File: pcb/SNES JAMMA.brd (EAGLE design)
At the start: 66 x 63.5 mm, 10 parts, among them P1-JAMMA-A PLAYER 1 JAMMA, P2-JAMMA-A PLAYER 2 JAMMA

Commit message: v1.0 PCB and Schematics files
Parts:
- removed P1-JAMMA-A: PLAYER 1 JAMMA, con-amp:10X05MTA
- removed P1-JAMMA-B, P2-JAMMA-B: (no value), con-amp:10X06MTA
- removed P2-JAMMA-A: PLAYER 2 JAMMA, con-amp:10X05MTA
- added J1: 12V POWER, con-amp:10X02MTA
- added J2: (no value), con-amp:10X03MTA
- added JAMMA: 057-040-1, con-panduit:057-040-1
- moved CPS1-KICK 59.5 mm to (8.89, 24.1), turned to 90 degrees
- moved EZ-KICK 52.6 mm to (8.89, 49.5), turned to 90 degrees
- moved SFC-PLAYER-1 51.2 mm to (30.5, 5.08), turned to 180 degrees
- moved SFC-PLAYER-2 49.6 mm to (45.7, 5.08), turned to 180 degrees
- moved PLAYER-2 20.7 mm to (43.2, 30.5)
- moved PLAYER-1 18.2 mm to (22.9, 30.5)
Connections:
- net P1-H-KICK renamed P1-BTN6
- net P1-L-KICK renamed P1-BTN4
- net P1-M-KICK renamed P1-BTN5
- net P2-H-KICK renamed P2-BTN6
- net P2-L-KICK renamed P2-BTN4
- net P2-M-KICK renamed P2-BTN5
- removed net P1-JAMMA-COIN: P1-JAMMA-B.5, PLAYER-1.J1.14
- removed net P1-JAMMA-DOWN: P1-JAMMA-A.3, PLAYER-1.J1.7
- removed net P1-JAMMA-H-PUNCH: P1-JAMMA-B.3, PLAYER-1.J1.12
- removed net P1-JAMMA-L-PUNCH: P1-JAMMA-B.1, PLAYER-1.J1.10
- removed net P1-JAMMA-LEFT: P1-JAMMA-A.4, PLAYER-1.J1.8
- removed net P1-JAMMA-M-PUNCH: P1-JAMMA-B.2, PLAYER-1.J1.11
- removed net P1-JAMMA-RIGHT: P1-JAMMA-A.5, PLAYER-1.J1.9
- removed net P1-JAMMA-START: P1-JAMMA-B.4, PLAYER-1.J1.13
- removed net P1-JAMMA-UP: P1-JAMMA-A.2, PLAYER-1.J1.6
- removed net P2-JAMMA-COIN: P2-JAMMA-B.2, PLAYER-2.J1.14
- removed net P2-JAMMA-DOWN: P2-JAMMA-A.3, PLAYER-2.J1.7
- removed net P2-JAMMA-H-PUNCH: P2-JAMMA-B.4, PLAYER-2.J1.12
- removed net P2-JAMMA-L-PUNCH: P2-JAMMA-B.6, PLAYER-2.J1.10
- removed net P2-JAMMA-LEFT: P2-JAMMA-A.2, PLAYER-2.J1.8
- removed net P2-JAMMA-M-PUNCH: P2-JAMMA-B.5, PLAYER-2.J1.11
- removed net P2-JAMMA-RIGHT: P2-JAMMA-A.1, PLAYER-2.J1.9
- removed net P2-JAMMA-START: P2-JAMMA-B.3, PLAYER-2.J1.13
- removed net P2-JAMMA-UP: P2-JAMMA-A.4, PLAYER-2.J1.6
- new net +12V: J1.2, J2.1
- new net N$6: PLAYER-1.J1.15
- new net P1-BTN1: JAMMA.27, PLAYER-1.J1.12
- new net P1-BTN2: JAMMA.29, PLAYER-1.J1.13
- new net P1-BTN3: JAMMA.31, PLAYER-1.J1.14
- new net P1-COIN: JAMMA.15, PLAYER-1.J1.6
- new net P1-DOWN: JAMMA.21, PLAYER-1.J1.9
- new net P1-LEFT: JAMMA.23, PLAYER-1.J1.10
- new net P1-RIGHT: JAMMA.25, PLAYER-1.J1.11
- new net P1-START: JAMMA.17, PLAYER-1.J1.7
- new net P1-UP: JAMMA.19, PLAYER-1.J1.8
- new net P2-BTN1: JAMMA.28, PLAYER-2.J1.12
- new net P2-BTN2: JAMMA.30, PLAYER-2.J1.13
- new net P2-BTN3: JAMMA.32, PLAYER-2.J1.14
- new net P2-COIN: JAMMA.16, PLAYER-2.J1.6
- new net P2-DOWN: JAMMA.22, PLAYER-2.J1.9
- new net P2-LEFT: JAMMA.24, PLAYER-2.J1.10
- new net P2-RIGHT: JAMMA.26, PLAYER-2.J1.11
- new net P2-START: JAMMA.18, PLAYER-2.J1.7
- new net P2-UP: JAMMA.20, PLAYER-2.J1.8
- net GND: now also J1.1, J2.2; no longer P1-JAMMA-B.6, P2-JAMMA-B.1
- net VCC: now also J2.3; no longer P1-JAMMA-A.1, P2-JAMMA-A.5
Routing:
- net VCC: track 267.2 -> 120.6 mm
- net P2-JAMMA-DOWN: track 55.2 -> 0.00 mm
- net P2-JAMMA-UP: track 53.8 -> 0.00 mm
- net P2-JAMMA-LEFT: track 52.3 -> 0.00 mm
- net P2-JAMMA-COIN: track 52.3 -> 0.00 mm
- net P2-JAMMA-H-PUNCH: track 52.3 -> 0.00 mm
- net P2-JAMMA-START: track 52.3 -> 0.00 mm
- net P2-JAMMA-RIGHT: track 52.3 -> 0.00 mm
- net P2-JAMMA-M-PUNCH: track 52.3 -> 0.00 mm
- net P2-JAMMA-L-PUNCH: track 52.3 -> 0.00 mm
- net P1-BTN6: track 60.6 -> 26.2 mm
- net P1-BTN4: track 63.2 -> 29.9 mm, vias 1 -> 0
- net P1-BTN5: track 62.2 -> 29.6 mm, vias 2 -> 0
- net P1-COIN: track 0.00 -> 31.5 mm
- net P1-BTN3: track 0.00 -> 31.5 mm
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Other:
- board text added: "+12V"
- board text added: "+5V"
- board text added: "CLK"
- board text added: "DTA"
- board text added: "EZ JAMMA SWITCHER"
- board text added: "LCH"
- board text added: "PLAYER 1"
- board text added: "PLAYER 2"
- board text added: "SFC TO JAMMA v1.0"
- board text removed: "5V"
- board text removed: "CLOCK"
- board text removed: "COIN"
- board text removed: "D"
- board text removed: "DATA"
- board text removed: "HP"
- board text removed: "L"
- board text removed: "LATCH"
- board text removed: "LP"
- board text removed: "MP"
- board text removed: "N/C"
- board text removed: "P1HK"
- board text removed: "P1LK"
- board text removed: "P1MK"
- board text removed: "P2HK"
- board text removed: "P2LK"
- board text removed: "P2MK"
- board text removed: "R"
- board text removed: "SFC TO JAMMA v0.1"
- board text removed: "START"
- board text removed: "U"

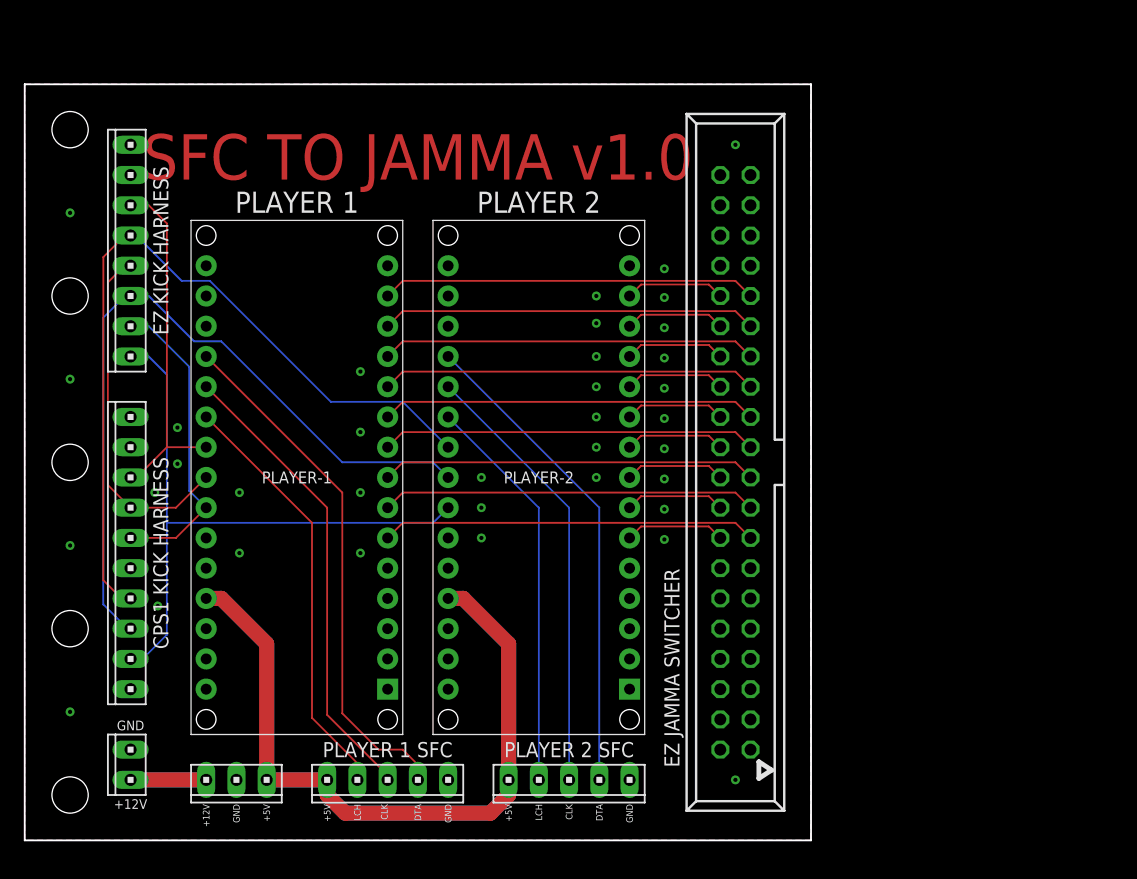
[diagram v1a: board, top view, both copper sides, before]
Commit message: Updating board design to v1.1 Adding ability for P1 Arduino to trigger "test" switch
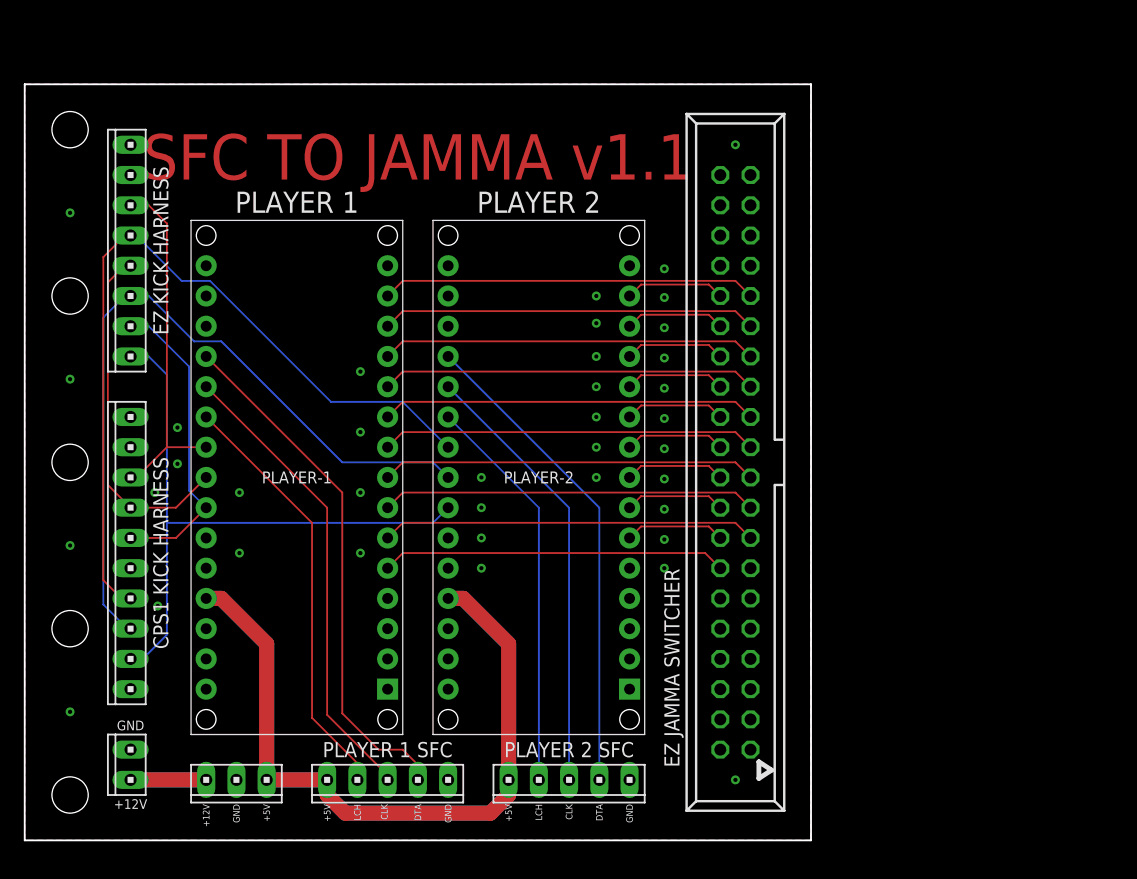
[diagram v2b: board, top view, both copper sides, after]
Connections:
- removed net N$3: PLAYER-1.J1.5
- new net TEST: JAMMA.14, PLAYER-1.J1.5
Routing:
- net TEST: track 0.00 -> 29.0 mm
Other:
- board text added: "SFC TO JAMMA v1.1"
- board text removed: "SFC TO JAMMA v1.0"
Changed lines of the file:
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@@
 <setting verticaltext="up"/>
 </settings>
-<grid distance="10" unitdist="mil" unit="mil" style="dots" multiple="1" display="yes" altdistance="5" altunitdist="mil" altunit="mil"/>
+<grid distance="5" unitdist="mil" unit="mil" style="dots" multiple="1" display="yes" altdistance="5" altunitdist="mil" altunit="mil"/>
 <layers>
 <layer number="1" name="Top" color="4" fill="1" visible="yes" active="yes"/>
@@
 <wire x1="66.04" y1="63.5" x2="66.04" y2="0" width="0.1524" layer="20"/>
 <wire x1="66.04" y1="0" x2="0" y2="0" width="0.1524" layer="20"/>
-<text x="33.02" y="57.404" size="3.81" layer="1" font="vector" ratio="15" align="center">SFC TO JAMMA v1.0</text>
+<text x="33.02" y="57.404" size="3.81" layer="1" font="vector" ratio="15" align="center">SFC TO JAMMA v1.1</text>
 <hole x="3.81" y="3.81" drill="3.048"/>
 <hole x="3.81" y="59.69" drill="3.048"/>
@@
 <via x="28.194" y="29.21" extent="1-16" drill="0.35"/>
 <via x="28.194" y="24.13" extent="1-16" drill="0.35"/>
+<via x="38.354" y="22.86" extent="1-16" drill="0.35"/>
+<via x="53.721" y="22.86" extent="1-16" drill="0.35"/>
 </signal>
 <signal name="P1-LED">
@@
 <contactref element="PLAYER-1" pad="J2.3"/>
 </signal>
-<signal name="N$3">
+<signal name="TEST">
 <contactref element="PLAYER-1" pad="J1.5"/>
+<contactref element="JAMMA" pad="14"/>
+<wire x1="30.48" y1="22.86" x2="31.75" y2="24.13" width="0.1524" layer="1"/>
+<wire x1="57.15" y1="24.13" x2="58.42" y2="22.86" width="0.1524" layer="1"/>
+<wire x1="31.75" y1="24.13" x2="57.15" y2="24.13" width="0.1524" layer="1"/>
 </signal>
 <signal name="N$4">

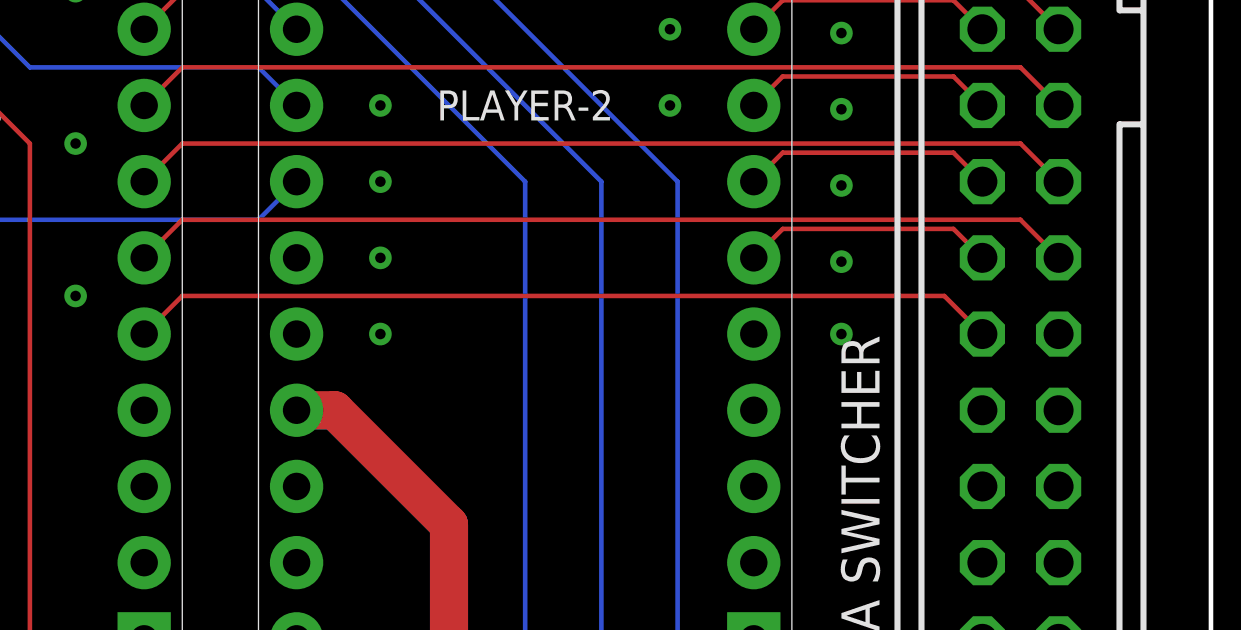
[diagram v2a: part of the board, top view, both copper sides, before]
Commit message: Correcting P1 TEST toggle incorrectly being wired to TILT instead P1 TEST is now properly TEST toggle Additionally, P2's is now wired into TILT so they're both available to be used!
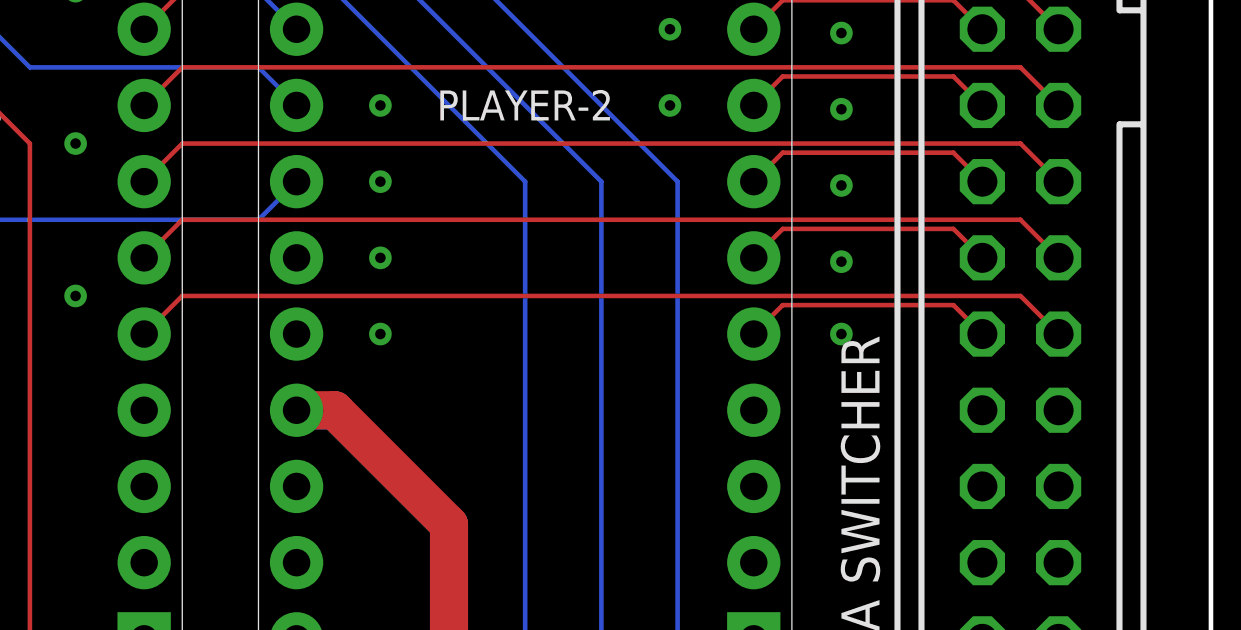
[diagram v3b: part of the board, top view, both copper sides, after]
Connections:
- removed net N$11: PLAYER-2.J1.5
- new net TILT: JAMMA.14, PLAYER-2.J1.5
- net TEST: now also JAMMA.13; no longer JAMMA.14
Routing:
- net TILT: track 0.00 -> 8.42 mm
- net TEST: track 29.0 -> 31.5 mm
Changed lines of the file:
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@@
 <layer number="27" name="tValues" color="7" fill="1" visible="yes" active="yes"/>
 <layer number="28" name="bValues" color="7" fill="1" visible="yes" active="yes"/>
-<layer number="29" name="tStop" color="7" fill="3" visible="no" active="yes"/>
-<layer number="30" name="bStop" color="7" fill="6" visible="no" active="yes"/>
+<layer number="29" name="tStop" color="7" fill="3" visible="yes" active="yes"/>
+<layer number="30" name="bStop" color="7" fill="6" visible="yes" active="yes"/>
 <layer number="31" name="tCream" color="7" fill="4" visible="no" active="yes"/>
 <layer number="32" name="bCream" color="7" fill="5" visible="no" active="yes"/>
@@
 <layer number="155" name="FabDoc3" color="7" fill="15" visible="no" active="no"/>
 <layer number="199" name="Contour" color="7" fill="1" visible="no" active="yes"/>
-<layer number="200" name="200bmp" color="1" fill="10" visible="no" active="yes"/>
+<layer number="200" name="200bmp" color="1" fill="10" visible="yes" active="yes"/>
 <layer number="201" name="201bmp" color="2" fill="1" visible="no" active="no"/>
 <layer number="202" name="202bmp" color="3" fill="1" visible="no" active="no"/>
@@
 <contactref element="PLAYER-1" pad="J2.3"/>
 </signal>
-<signal name="TEST">
-<contactref element="PLAYER-1" pad="J1.5"/>
-<contactref element="JAMMA" pad="14"/>
-<wire x1="30.48" y1="22.86" x2="31.75" y2="24.13" width="0.1524" layer="1"/>
-<wire x1="57.15" y1="24.13" x2="58.42" y2="22.86" width="0.1524" layer="1"/>
-<wire x1="31.75" y1="24.13" x2="57.15" y2="24.13" width="0.1524" layer="1"/>
-</signal>
 <signal name="N$4">
 <contactref element="PLAYER-1" pad="J1.2"/>
@@
 <contactref element="PLAYER-2" pad="J2.5"/>
 </signal>
-<signal name="N$11">
+<signal name="TILT">
 <contactref element="PLAYER-2" pad="J1.5"/>
+<contactref element="JAMMA" pad="14"/>
+<wire x1="50.8" y1="22.86" x2="51.7652" y2="23.8252" width="0.1524" layer="1"/>
+<wire x1="57.4548" y1="23.8252" x2="58.42" y2="22.86" width="0.1524" layer="1"/>
+<wire x1="51.7652" y1="23.8252" x2="57.4548" y2="23.8252" width="0.1524" layer="1"/>
 </signal>
 <signal name="N$12">
@@
 <wire x1="8.89" y1="5.08" x2="15.24" y2="5.08" width="1.27" layer="1"/>
 </signal>
+<signal name="TEST">
+<contactref element="PLAYER-1" pad="J1.5"/>
+<contactref element="JAMMA" pad="13"/>
+<wire x1="30.48" y1="22.86" x2="31.75" y2="24.13" width="0.1524" layer="1"/>
+<wire x1="59.69" y1="24.13" x2="60.96" y2="22.86" width="0.1524" layer="1"/>
+<wire x1="31.75" y1="24.13" x2="59.69" y2="24.13" width="0.1524" layer="1"/>
+</signal>
 </signals>
